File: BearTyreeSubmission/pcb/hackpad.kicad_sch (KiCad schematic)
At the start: 26 parts, among them J1 OLED_128x32, SW13 RotaryEncoder_Switch, U1 MOUDLE-SEEEDUINO-XIAO

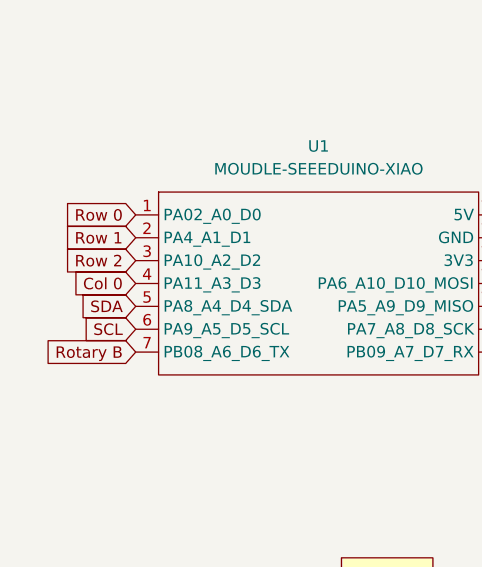
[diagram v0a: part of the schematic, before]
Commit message: Fixed USBC Hole
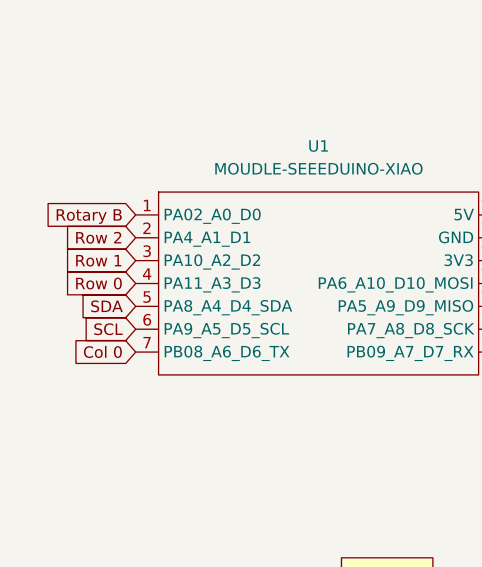
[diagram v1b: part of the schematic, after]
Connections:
- net Col 0: now also U1.7 (PB08_A6_D6_TX); no longer U1.4 (PA11_A3_D3)
- net Rotary B: now also U1.1 (PA02_A0_D0); no longer U1.7 (PB08_A6_D6_TX)
- net Row 0: now also U1.4 (PA11_A3_D3); no longer U1.1 (PA02_A0_D0)
- net Row 1: now also U1.3 (PA10_A2_D2); no longer U1.2 (PA4_A1_D1)
- net Row 2: now also U1.2 (PA4_A1_D1); no longer U1.3 (PA10_A2_D2)
